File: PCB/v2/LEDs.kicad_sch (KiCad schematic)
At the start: 8 parts

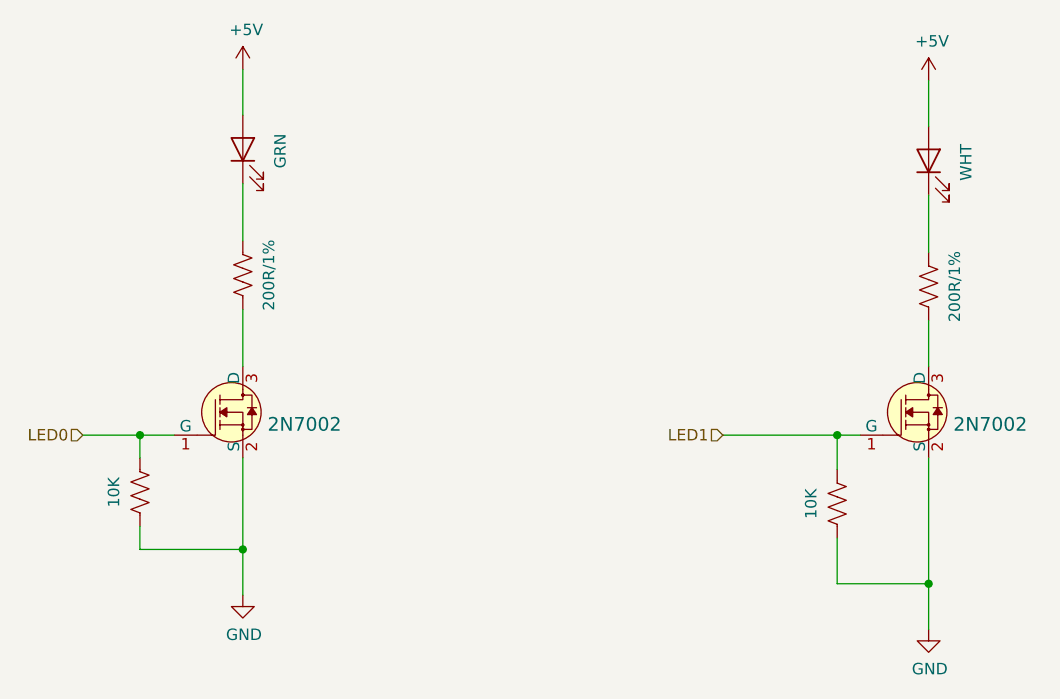
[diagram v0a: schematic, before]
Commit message: WIP updated symbols for tmc5106
Updated footprint for tmc5106,
need to check how motor wiring is done, might be wired up stupid before and that's gonna be sad
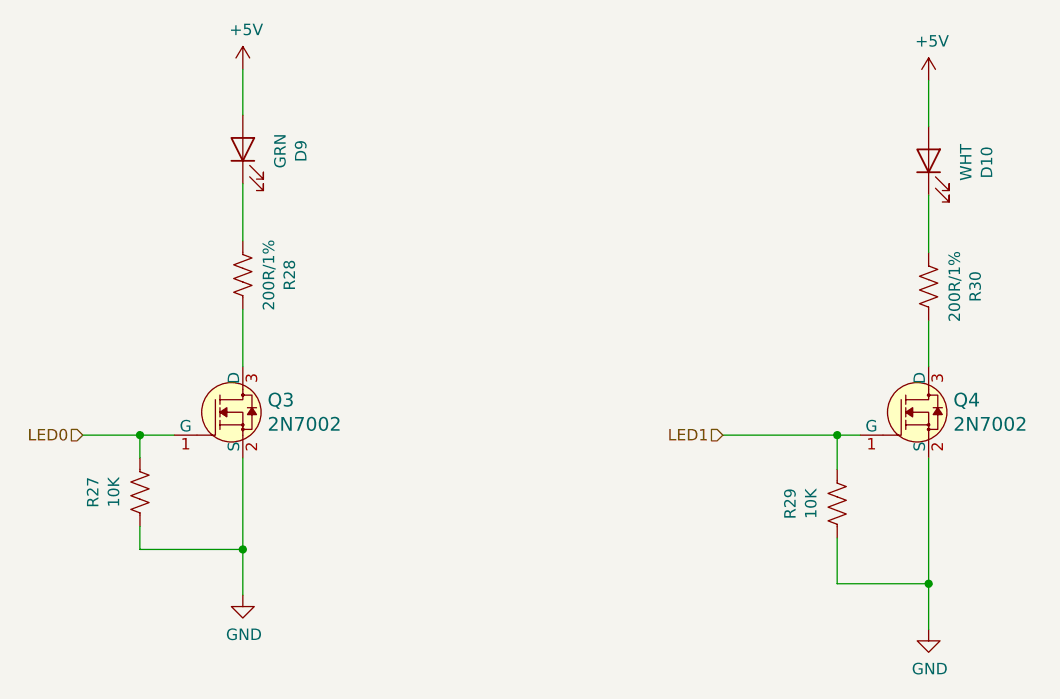
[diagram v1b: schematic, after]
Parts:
- gave numbers to parts that had none: 8
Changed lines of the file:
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@@
   (symbol (lib_id "MMTK-rescue:LED-Device-MMTK-rescue-MMTK-rescue") (at 101.6 49.53 90) (unit 1)
     (in_bom yes) (on_board yes)
-    (property "Reference" "" (id 0) (at 108.077 49.7078 0))
+    (property "Reference" "D9" (id 0) (at 108.077 49.7078 0))
     (property "Value" "GRN" (id 1) (at 105.7656 49.7078 0))
     (property "Footprint" "LED_SMD:LED_0603_1608Metric" (id 2) (at 101.6 49.53 0)
@@
   (symbol (lib_id "MMTK-rescue:+5V-power-MMTK-rescue-MMTK-rescue") (at 101.6 40.64 0) (unit 1)
     (in_bom yes) (on_board yes)
-    (property "Reference" "" (id 0) (at 101.6 44.45 0)
+    (property "Reference" "#PWR0153" (id 0) (at 101.6 44.45 0)
       (effects (font (size 1.27 1.27)) hide)
     )
@@
   (symbol (lib_id "MMTK-rescue:R_US-Device-MMTK-rescue-MMTK-rescue") (at 101.6 63.5 180) (unit 1)
     (in_bom yes) (on_board yes)
-    (property "Reference" "" (id 0) (at 106.807 63.5 90))
+    (property "Reference" "R28" (id 0) (at 106.807 63.5 90))
     (property "Value" "200R/1%" (id 1) (at 104.4956 63.5 90))
     (property "Footprint" "Resistor_SMD:R_0603_1608Metric" (id 2) (at 100.584 63.246 90)
@@
   (symbol (lib_id "MMTK-rescue:R_US-Device-MMTK-rescue-MMTK-rescue") (at 177.8 64.77 180) (unit 1)
     (in_bom yes) (on_board yes)
-    (property "Reference" "" (id 0) (at 183.007 64.77 90))
+    (property "Reference" "R30" (id 0) (at 183.007 64.77 90))
     (property "Value" "200R/1%" (id 1) (at 180.6956 64.77 90))
     (property "Footprint" "Resistor_SMD:R_0603_1608Metric" (id 2) (at 176.784 64.516 90)
@@
   (symbol (lib_id "MMTK-rescue:GND-power-MMTK-rescue-MMTK-rescue") (at 101.6 99.06 0) (unit 1)
     (in_bom yes) (on_board yes)
-    (property "Reference" "" (id 0) (at 101.6 105.41 0)
+    (property "Reference" "#PWR0154" (id 0) (at 101.6 105.41 0)
       (effects (font (size 1.27 1.27)) hide)
     )
@@
   (symbol (lib_id "MMTK-rescue:LED-Device-MMTK-rescue-MMTK-rescue") (at 177.8 50.8 90) (unit 1)
     (in_bom yes) (on_board yes)
-    (property "Reference" "" (id 0) (at 184.277 50.9778 0))
+    (property "Reference" "D10" (id 0) (at 184.277 50.9778 0))
     (property "Value" "WHT" (id 1) (at 181.9656 50.9778 0))
     (property "Footprint" "LED_SMD:LED_0603_1608Metric" (id 2) (at 177.8 50.8 0)
@@
   (symbol (lib_id "MMTK-rescue:+5V-power-MMTK-rescue-MMTK-rescue") (at 177.8 41.91 0) (unit 1)
     (in_bom yes) (on_board yes)
-    (property "Reference" "" (id 0) (at 177.8 45.72 0)
+    (property "Reference" "#PWR0155" (id 0) (at 177.8 45.72 0)
       (effects (font (size 1.27 1.27)) hide)
     )
@@
   (symbol (lib_id "MMTK-rescue:GND-power-MMTK-rescue-MMTK-rescue") (at 177.8 102.87 0) (unit 1)
     (in_bom yes) (on_board yes)
-    (property "Reference" "" (id 0) (at 177.8 109.22 0)
+    (property "Reference" "#PWR0156" (id 0) (at 177.8 109.22 0)
       (effects (font (size 1.27 1.27)) hide)
     )
@@
   (symbol (lib_id "MMTK-rescue:R_US-Device-MMTK-rescue-MMTK-rescue") (at 90.17 87.63 0) (unit 1)
     (in_bom yes) (on_board yes)
-    (property "Reference" "" (id 0) (at 84.963 87.63 90))
+    (property "Reference" "R27" (id 0) (at 84.963 87.63 90))
     (property "Value" "10K" (id 1) (at 87.2744 87.63 90))
     (property "Footprint" "Resistor_SMD:R_0603_1608Metric" (id 2) (at 91.186 87.884 90)
@@
   (symbol (lib_id "MMTK-rescue:R_US-Device-MMTK-rescue-MMTK-rescue") (at 167.64 88.9 0) (unit 1)
     (in_bom yes) (on_board yes)
-    (property "Reference" "" (id 0) (at 162.433 88.9 90))
+    (property "Reference" "R29" (id 0) (at 162.433 88.9 90))
     (property "Value" "10K" (id 1) (at 164.7444 88.9 90))
     (property "Footprint" "Resistor_SMD:R_0603_1608Metric" (id 2) (at 168.656 89.154 90)
@@
   (symbol (lib_id "dk_Transistors-FETs-MOSFETs-Single:2N7002") (at 101.6 78.74 0) (unit 1)
     (in_bom yes) (on_board yes)
-    (property "Reference" "" (id 0) (at 104.3432 77.3938 0)
+    (property "Reference" "Q3" (id 0) (at 104.3432 77.3938 0)
       (effects (font (size 1.524 1.524)) (justify left))
     )
@@
   (symbol (lib_id "dk_Transistors-FETs-MOSFETs-Single:2N7002") (at 177.8 78.74 0) (unit 1)
     (in_bom yes) (on_board yes)
-    (property "Reference" "" (id 0) (at 180.5432 77.3938 0)
+    (property "Reference" "Q4" (id 0) (at 180.5432 77.3938 0)
       (effects (font (size 1.524 1.524)) (justify left))
     )
